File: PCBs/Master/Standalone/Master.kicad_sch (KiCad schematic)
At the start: 28 parts

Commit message: Master WIP
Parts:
- removed BUS1, BUS2, BUS3: Conn_02x04_Top_Bottom, A10 KiCad Libraries:Molex 43045-0800, symbol Connector_Generic:Conn_02x04_Top_Bottom
- removed C1: 0.1uF, A10 KiCad Libraries:FA14, symbol Device:C
- removed D3: GREEN, LED_SMD:LED_1210_3225Metric_Pad1.42x2.65mm_HandSolder, symbol Device:LED
- removed F1, F2, F3: 6A, A10 KiCad Libraries:FUSE_BK-6013, symbol Device:Fuse
- removed MASTER-1, MASTER-2, MASTER-3: MAX487CPA+, Package_DIP:DIP-8_W7.62mm_LongPads, symbol A10:MAX487CPA+
- removed MEGA-1, MEGA-2: Conn_01x06_Male, A10 KiCad Libraries:SHDR6W64P0X250_1X6_1740X575X700P, symbol Connector:Conn_01x06_Male
- removed PSU1, PSU2, PSU3: Conn_02x02_Top_Bottom, A10 KiCad Libraries:Molex 43045-0400, symbol Connector_Generic:Conn_02x02_Odd_Even
- added C1: 4.7uF, A10 KiCad Libraries:C0805, symbol Device:C_Polarized
- added C12, C7, C8: 100nF, A10 KiCad Libraries:C0402, symbol Device:C
- added C13: 10uF, A10 KiCad Libraries:C0402, symbol Device:C
- added C14, C4, C5, C6: 1uF, A10 KiCad Libraries:C0402, symbol Device:C
- added C15, C16: 15pF, A10 KiCad Libraries:C0402, symbol Device:C
- added D3: DIODE, A10 KiCad Libraries:SOD-123_L2.7-W1.6-LS3.7-RD-1, symbol pspice:DIODE
- added D5: LED, LED_SMD:LED_0603_1608Metric, symbol Device:LED
- added H1, H2, H3, H4: MountingHole, MountingHole:MountingHole_3.2mm_M3, symbol Mechanical:MountingHole
- added J1: Conn_01x06_Female, Connector_PinSocket_2.54mm:PinSocket_1x06_P2.54mm_Vertical, symbol Connector:Conn_01x06_Female
- added J2: AVR-ISP-6, Connector_PinHeader_2.54mm:PinHeader_2x03_P2.54mm_Vertical, symbol Connector:AVR-ISP-6
- added J3: USB_B_Micro, A10 KiCad Libraries:MICRO-USB-SMD_U254-051T-4BHJ25-F2S, symbol Connector:USB_B_Micro
- added R8: 1K, Resistor_SMD:R_0805_2012Metric, symbol Device:R
- added SW1: SW_MEC_5E, A10 KiCad Libraries:SW-SMD_4P-L5.1-W5.1-P3.70-LS6.5-TL-2, symbol Switch:SW_MEC_5E
- added SW2: SW_DIP_x01, A10 KiCad Libraries:SW-SMD_DSHP02TSGER, symbol Switch:SW_DIP_x02
- added U2: ATmega2560-16A, Package_QFP:TQFP-100_14x14mm_P0.5mm, symbol MCU_Microchip_ATmega:ATmega2560-16A
- added U3: CH340C, A10 KiCad Libraries:SOP-16_L10.0-W3.9-P1.27-LS6.0-BL, symbol Interface_USB:CH340C
- added Y1: Crystal_GND24, Crystal:Crystal_SMD_3225-4Pin_3.2x2.5mm, symbol Device:Crystal_GND24
- C2, C3: value 0.1uF -> 1uF; footprint A10 KiCad Libraries:FA14 -> A10 KiCad Libraries:C0402; LCSC (none) -> C52923
- D1: value GREEN -> LED; footprint LED_SMD:LED_1210_3225Metric_Pad1.42x2.65mm_HandSolder -> LED_SMD:LED_0603_1608Metric; Field4 12V_1 -> (none); LCSC (none) -> C72041
- D2: value GREEN -> LED; footprint LED_SMD:LED_1210_3225Metric_Pad1.42x2.65mm_HandSolder -> LED_SMD:LED_0603_1608Metric; Field4 12V_2 -> (none); LCSC (none) -> C72041
- D4: value GREEN -> LED; footprint LED_SMD:LED_1210_3225Metric_Pad1.42x2.65mm_HandSolder -> LED_SMD:LED_0603_1608Metric; Field4 5V -> (none); LCSC (none) -> C72041
- R1: value 120Ω -> 10K; footprint Resistor_THT:R_Axial_DIN0207_L6.3mm_D2.5mm_P7.62mm_Horizontal -> Resistor_SMD:R_0805_2012Metric; LCSC (none) -> C17414
- R2, R3: value 120Ω -> 1K; footprint Resistor_THT:R_Axial_DIN0207_L6.3mm_D2.5mm_P7.62mm_Horizontal -> Resistor_SMD:R_0805_2012Metric; LCSC (none) -> C17513
- R4, R5, R6: value 1.8K -> 1K; footprint Resistor_SMD:R_1210_3225Metric_Pad1.30x2.65mm_HandSolder -> Resistor_SMD:R_0805_2012Metric; LCSC (none) -> C17513
- R7: value 400R -> 1K; footprint Resistor_SMD:R_1210_3225Metric_Pad1.30x2.65mm_HandSolder -> Resistor_SMD:R_0805_2012Metric; LCSC (none) -> C17513
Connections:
- net RS485-1-B is gone; now on net +5V: R1.1
- net RS485-3-A is gone; now on an unnamed net: R3.2
- net RS485-3-B is gone; now on net +5V: R3.1
- net +5V: now also C2.1, C3.1, C1.1, C14.1, C4.1, C5.1, C6.1, D3.2 (A), J1.4 (Pin_4), J2.2 (VCC), R8.2, SW2.4, U2.10 (VCC), U2.100 (AVCC), U2.31 (VCC), U2.61 (VCC), U2.80 (VCC); no longer C2.2, C3.2
- net GND: now also C2.2, C3.2, D1.1 (K), D2.1 (K), C1.2, C12.1, C13.1, C15.1, C16.2, C4.2, C5.2, C6.2, C8.1, J1.5 (Pin_5), J1.6 (Pin_6), J2.6 (GND), J3.5 (GND), J3.6 (Shield), SW1.1, SW1.2, U2.11 (GND), U2.32 (GND), U2.62 (GND), U2.81 (GND), U2.99 (GND), U3.1 (GND), Y1.2, Y1.4; no longer C2.1, C3.1, D4.1 (K)
- net at D2.2 (A): no longer R5.1
- net at R6.1: now also U3.3 (RXD)
- net at R4.1: now also SW2.1; no longer D1.2 (A)
- net 12V_2_Fused renamed USB_TXD
- net USB_TXD: now also D4.1 (K), J1.3 (Pin_3), U2.2 (PE0/RXD0/~D0)
- net 12V_3_Fused renamed USB_RXD
- net USB_RXD: now also D5.1 (K), J1.2 (Pin_2), U2.3 (PE1/TXD0/~D1)
- net 12V_Fused renamed D2
- net D2: now also U2.6 (PE4/~D2)
- net RS485-1-A renamed RESET
- net RESET: now also C7.1, J2.5 (~{RST}), SW1.3 (K), SW1.4 (A), U2.30 (~{RESET})
- net RS485-2-A: no longer names the net of R2.2
- net RS485-2-A: now also D1.2 (A)
- net RS485-2-B renamed D13
- new net: C12.2, C13.2, D3.1 (K), J3.1 (VBUS)
- new net: C14.2, U3.16 (VCC)
- new net: D5.2 (A), R8.1
- new net: R5.1, U3.2 (TXD)
- new net: C8.2, U2.98 (AREF)
- new net D+: J3.3 (D+), U3.5 (UD+)
- new net D-: J3.2 (D-), U3.6 (UD-)
- new net D14: U2.64 (PJ1/TXD3/D14)
- new net D15: U2.63 (PJ0/RXD3/D15)
- new net D16: U2.13 (PH1/TXD2/D16)
- new net D17: U2.12 (PH0/RXD2/D17)
- new net D18: U2.46 (PD3/TXD1/D18)
- new net D19: U2.45 (PD2/RXD1/D19)
- new net D3: U2.7 (PE5/~D3)
- new net D4: U2.1 (PG5/~D4)
- new net D50: J2.1 (MISO), U2.22 (PB3/MISO/D50)
- new net D51: J2.4 (MOSI), U2.21 (PB2/MOSI/D51)
- new net D52: J2.3 (SCK), U2.20 (PB1/SCK/D52)
- new net FTDI_DTR: C7.2, J1.1 (Pin_1), U3.13 (~{DTR})
- new net XTAL1: C15.2, U2.34 (XTAL1), Y1.1
- new net XTAL2: C16.1, U2.33 (XTAL2), Y1.3
- no-connect marks 6 -> 77
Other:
- added sheet RS485-1 (RS485.kicad_sch)
- added sheet RS485-2 (RS485.kicad_sch)
- added sheet RS485-3 (RS485.kicad_sch)
- note added: "Configuration"
- note added: "Crystal"
- note added: "D13"
- note added: "Decoupling"
- note added: "FTDI Header"
- note added: "ICSP"
- note added: "PLED"
- note added: "RS485"
- note added: "RS485 Power Toggle"
- note added: "RS485 Termination"
- note added: "Reset"
- note added: "Standard LEDs"
- note added: "USB"
- note added: "USB LEDs"
- company: (none) -> Maciej Swic
- title: (none) -> DCS-BIOS Master

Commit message: Master WIP
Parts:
- removed R4: 1K, Resistor_SMD:R_0805_2012Metric, symbol Device:R
- removed SW2: SW_DIP_x01, A10 KiCad Libraries:SW-SMD_DSHP02TSGER, symbol Switch:SW_DIP_x02
- R2: renamed from R3; footprint Resistor_SMD:R_0805_2012Metric -> Resistor_SMD:R_0402_1005Metric; LCSC C17513 -> C11702
- R3: renamed from R2; footprint Resistor_SMD:R_0805_2012Metric -> Resistor_SMD:R_0402_1005Metric; LCSC C17513 -> C11702
- R5, R6, R7, R8: footprint Resistor_SMD:R_0805_2012Metric -> Resistor_SMD:R_0402_1005Metric; LCSC C17513 -> C11702
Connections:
- net D13: now also U2.26 (PB7/~D13)
- no-connect marks 77 -> 76
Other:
- note removed: "Configuration"
- note removed: "RS485 Power Toggle"
- note removed: "RS485 Termination"
- moved on the sheet: C12, C13, C14, D3, D4, D5, J3, R5, R6, R7, R8, U3

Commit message: Master Rev. 1
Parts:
- removed J1: Conn_01x06_Female, Connector_PinSocket_2.54mm:PinSocket_1x06_P2.54mm_Vertical, symbol Connector:Conn_01x06_Female
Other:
- note removed: "FTDI Header"
- moved on the sheet: C12, C13, C14, D1, D2, D3, D4, D5, J3, R2, R3, R5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

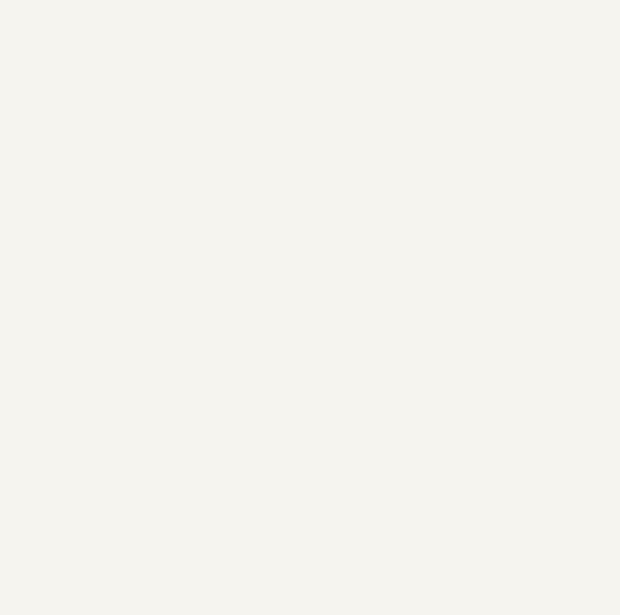
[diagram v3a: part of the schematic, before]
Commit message: Updated Master to use PCIe Power Directly
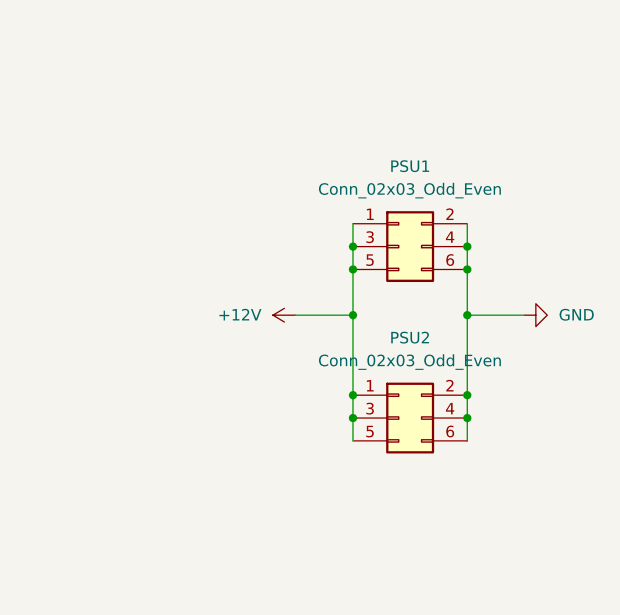
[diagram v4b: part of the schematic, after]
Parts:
- added PSU1, PSU2: Conn_02x03_Odd_Even, A10 KiCad Libraries:CONN-TH_HAA420A-6AW-C2845788, symbol Connector_Generic:Conn_02x03_Odd_Even
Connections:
- net GND: now also PSU1.2 (Pin_2), PSU1.4 (Pin_4), PSU1.6 (Pin_6), PSU2.2 (Pin_2), PSU2.4 (Pin_4), PSU2.6 (Pin_6)
- new net +12V: PSU1.1 (Pin_1), PSU1.3 (Pin_3), PSU1.5 (Pin_5), PSU2.1 (Pin_1), PSU2.3 (Pin_3), PSU2.5 (Pin_5)
